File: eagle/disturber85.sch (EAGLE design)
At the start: 4 parts, among them U1 ATTINY85, U2 ATTINY85-20P

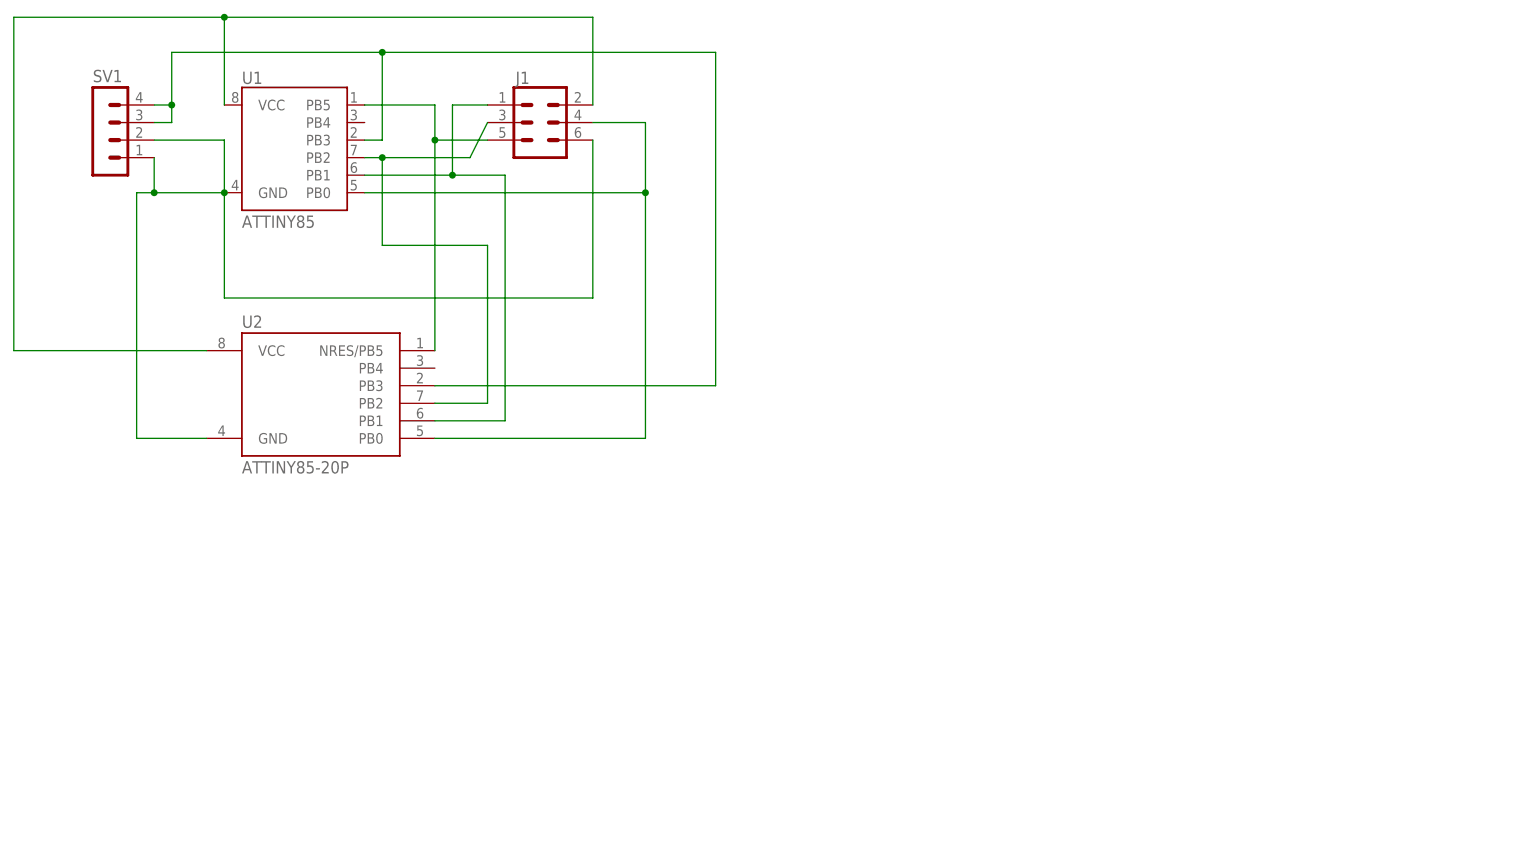
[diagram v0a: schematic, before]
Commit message: Panelized
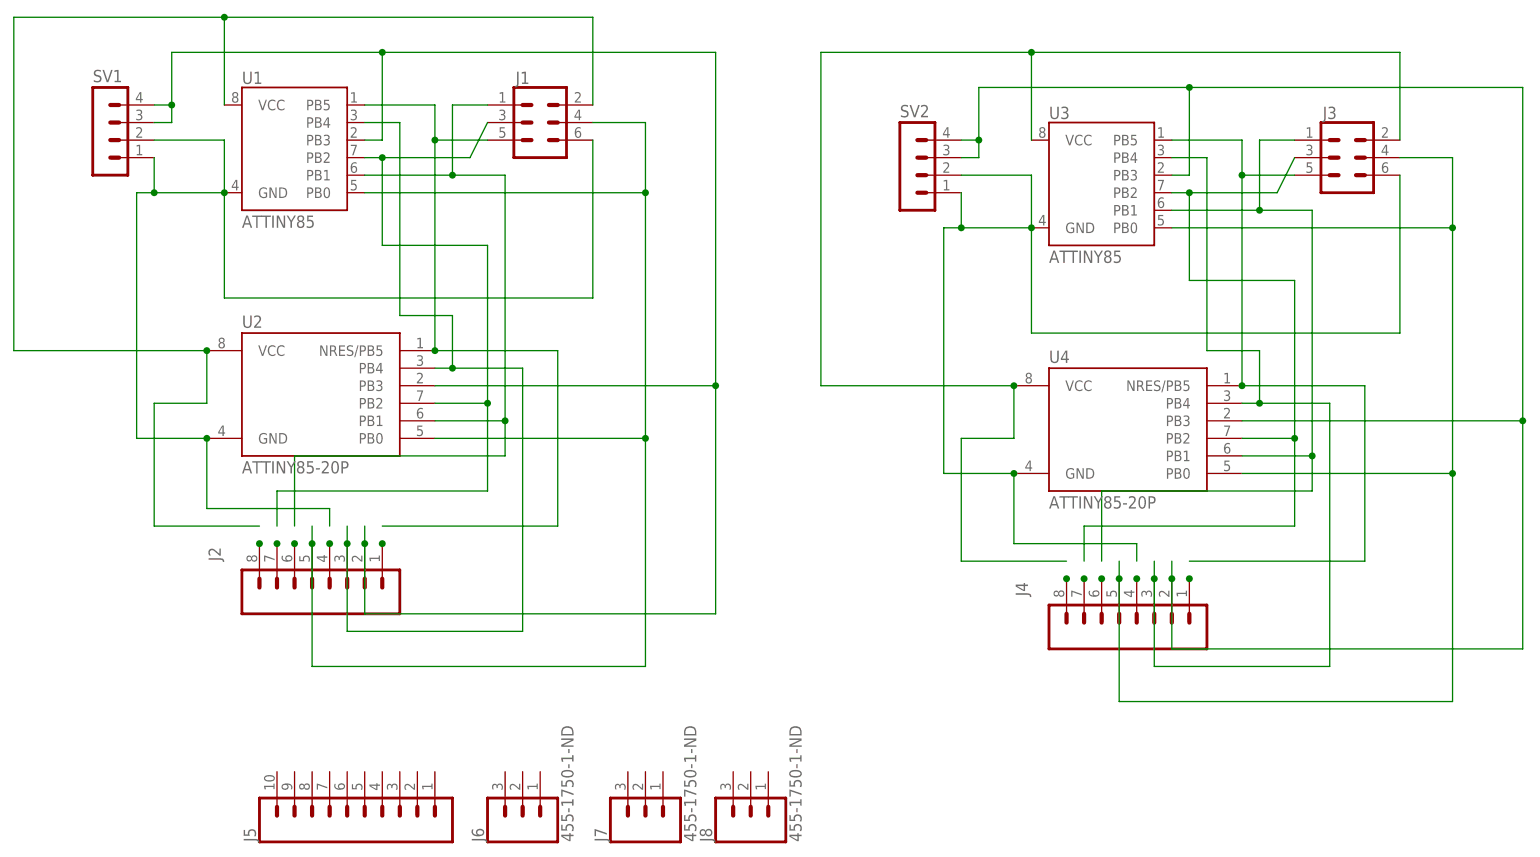
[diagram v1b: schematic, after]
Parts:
- added J2, J4: (no value), SparkFun-Connectors:CONN_08"
- added J3: (no value), SparkFun-Connectors:CONN_03X22X3_SILK_MALE_PTH
- added J5: (no value), SparkFun-Connectors:CONN_10"
- added J6, J7, J8: 455-1750-1-ND, SparkFun-Connectors:CONN_03
- added SV2: (no value), con-lstb:MA04-1
- added U3: ATTINY85, SparkFun-IC-Microcontroller:ATTINY85
- added U4: ATTINY85-20P, _hhn_attiny25_45_85:ATTINY85-20P
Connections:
- new net N$10: J3.2, J4.8, U3.VCC, U4.VCC
- new net N$11: J3.5, J4.1, U3.PB5, U4.NRES/PB5
- new net N$12: J3.4, J4.5, U3.PB0, U4.PB0
- new net N$13: J3.3, J4.7, U3.PB2, U4.PB2
- new net N$14: J3.1, J4.6, U3.PB1, U4.PB1
- new net N$15: J4.2, SV2.3, SV2.4, U3.PB3, U4.PB3
- new net N$16: J4.3, U3.PB4, U4.PB4
- new net N$8: J2.3, U1.PB4, U2.PB4
- new net N$9: J3.6, J4.4, SV2.1, SV2.2, U3.GND, U4.GND
- net N$1: now also J2.4
- net N$2: now also J2.8
- net N$3: now also J2.1
- net N$4: now also J2.5
- net N$5: now also J2.7
- net N$6: now also J2.6
- net N$7: now also J2.2

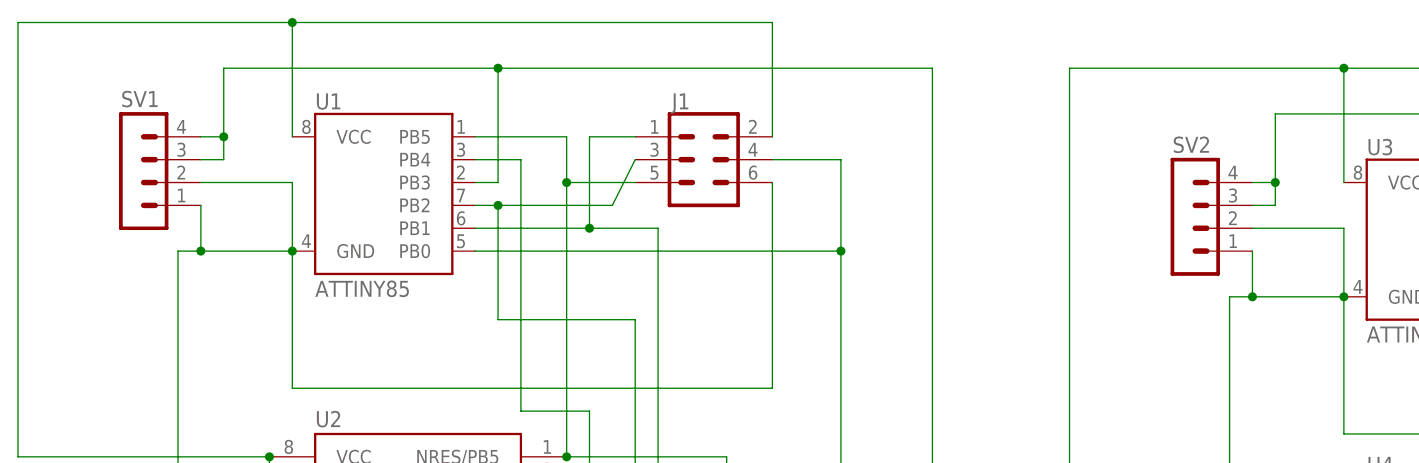
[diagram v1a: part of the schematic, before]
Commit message: Panelized
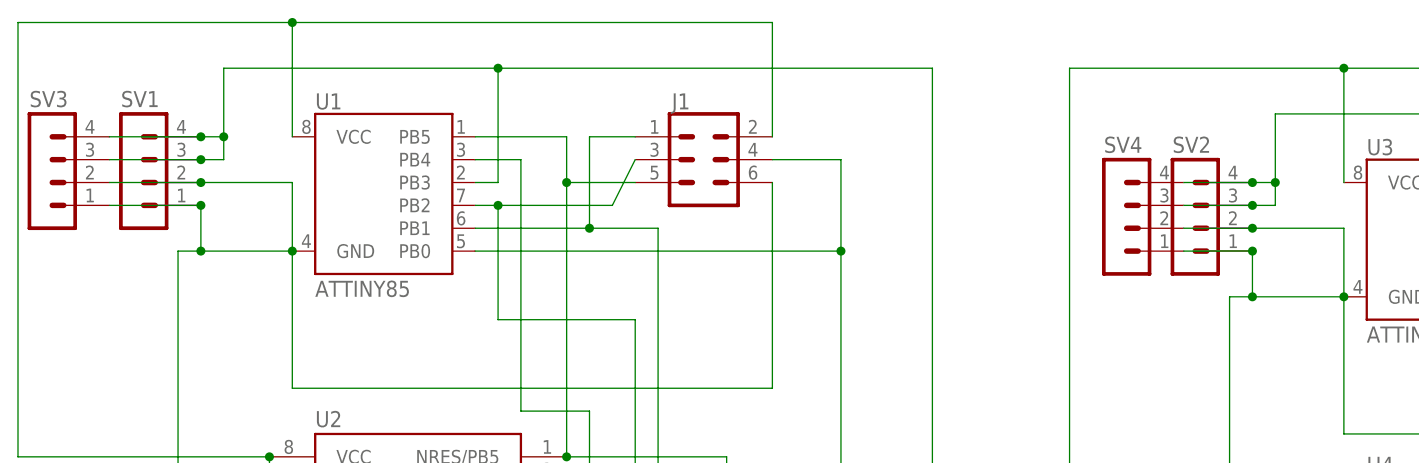
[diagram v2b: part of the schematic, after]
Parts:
- added SV3, SV4: (no value), con-lstb:MA04-1
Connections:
- net N$1: now also SV3.1, SV3.2
- net N$15: now also SV4.3, SV4.4
- net N$7: now also SV3.3, SV3.4
- net N$9: now also SV4.1, SV4.2
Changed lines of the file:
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@@
 <part name="J7" library="SparkFun-Connectors" deviceset="CONN_03" device="" value="455-1750-1-ND"/>
 <part name="J8" library="SparkFun-Connectors" deviceset="CONN_03" device="" value="455-1750-1-ND"/>
+<part name="SV3" library="con-lstb" library_urn="urn:adsk.eagle:library:162" deviceset="MA04-1" device="" package3d_urn="urn:adsk.eagle:package:8337/1"/>
+<part name="SV4" library="con-lstb" library_urn="urn:adsk.eagle:library:162" deviceset="MA04-1" device="" package3d_urn="urn:adsk.eagle:package:8337/1"/>
 </parts>
 <sheets>
@@
 <attribute name="VALUE" x="103.886" y="-68.58" size="1.778" layer="96" font="vector" rot="R90"/>
 <attribute name="NAME" x="90.932" y="-68.58" size="1.778" layer="95" font="vector" rot="R90"/>
+</instance>
+<instance part="SV3" gate="1" x="-7.62" y="35.56" smashed="yes">
+<attribute name="VALUE" x="-8.89" y="25.4" size="1.778" layer="96"/>
+<attribute name="NAME" x="-8.89" y="41.402" size="1.778" layer="95"/>
+</instance>
+<instance part="SV4" gate="1" x="111.76" y="30.48" smashed="yes">
+<attribute name="VALUE" x="110.49" y="20.32" size="1.778" layer="96"/>
+<attribute name="NAME" x="110.49" y="36.322" size="1.778" layer="95"/>
 </instance>
 </instances>
@@
 <wire x1="35.56" y1="-20.32" x2="35.56" y2="-22.86" width="0.1524" layer="91"/>
 <junction x="35.56" y="-25.4"/>
+<pinref part="SV3" gate="1" pin="2"/>
+<wire x1="0" y1="33.02" x2="10.16" y2="33.02" width="0.1524" layer="91"/>
+<junction x="10.16" y="33.02"/>
+<pinref part="SV3" gate="1" pin="1"/>
+<wire x1="0" y1="30.48" x2="10.16" y2="30.48" width="0.1524" layer="91"/>
+<junction x="10.16" y="30.48"/>
 </segment>
 </net>
@@
 <junction x="91.44" y="-2.54"/>
 <junction x="40.64" y="-25.4"/>
+<pinref part="SV3" gate="1" pin="4"/>
+<wire x1="0" y1="38.1" x2="10.16" y2="38.1" width="0.1524" layer="91"/>
+<junction x="10.16" y="38.1"/>
+<pinref part="SV3" gate="1" pin="3"/>
+<wire x1="0" y1="35.56" x2="10.16" y2="35.56" width="0.1524" layer="91"/>
+<junction x="10.16" y="35.56"/>
 </segment>
 </net>
@@
 <wire x1="152.4" y1="-25.4" x2="152.4" y2="-27.94" width="0.1524" layer="91"/>
 <junction x="152.4" y="-30.48"/>
+<pinref part="SV4" gate="1" pin="2"/>
+<wire x1="119.38" y1="27.94" x2="127" y2="27.94" width="0.1524" layer="91"/>
+<junction x="127" y="27.94"/>
+<pinref part="SV4" gate="1" pin="1"/>
+<wire x1="119.38" y1="25.4" x2="127" y2="25.4" width="0.1524" layer="91"/>
+<junction x="127" y="25.4"/>
 </segment>
 </net>
@@
 <junction x="208.28" y="-7.62"/>
 <junction x="157.48" y="-30.48"/>
-</segment>
-</net>
+<pinref part="SV4" gate="1" pin="4"/>
+<wire x1="119.38" y1="33.02" x2="127" y2="33.02" width="0.1524" layer="91"/>
+<junction x="127" y="33.02"/>
+<pinref part="SV4" gate="1" pin="3"/>
+<wire x1="119.38" y1="30.48" x2="127" y2="30.48" width="0.1524" layer="91"/>
+<junction x="127" y="30.48"/>
+</segment>
+</net>
